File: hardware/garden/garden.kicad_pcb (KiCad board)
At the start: 4 copper layers, 99.7 x 99.7 mm, 111 parts, among them J1 CONN_01X04, J10 CONN_01X09, J2 CONN_01X02, J3 CONN_01X02, J4 CONN_01X02, J5 CONN_01X02, J6 CONN_01X02, J7 CONN_01X04, J8 CONN_01X04, J9 USB_B_Micro, M2 CONN_01X01, M3 CONN_01X01, M4 CONN_01X01, M5 CONN_01X01, Q1 Q_NPN_BEC, Q2 Q_NMOS_GDS, Q3 Q_NMOS_GDS, Q4 Q_NPN_BEC, Q5 Q_NMOS_GDS, SW1 SW_Push, U1 INA226, U10 DHT11, U11 AZ1117-3.3, U12 MCP1416, U13 MCP1416, U14 MCP1416, U2 INA226, U3 CP2102, U4 ESP32-WROOM-32, U5 INA226, U7 MCP1416, U9 MP2451DT

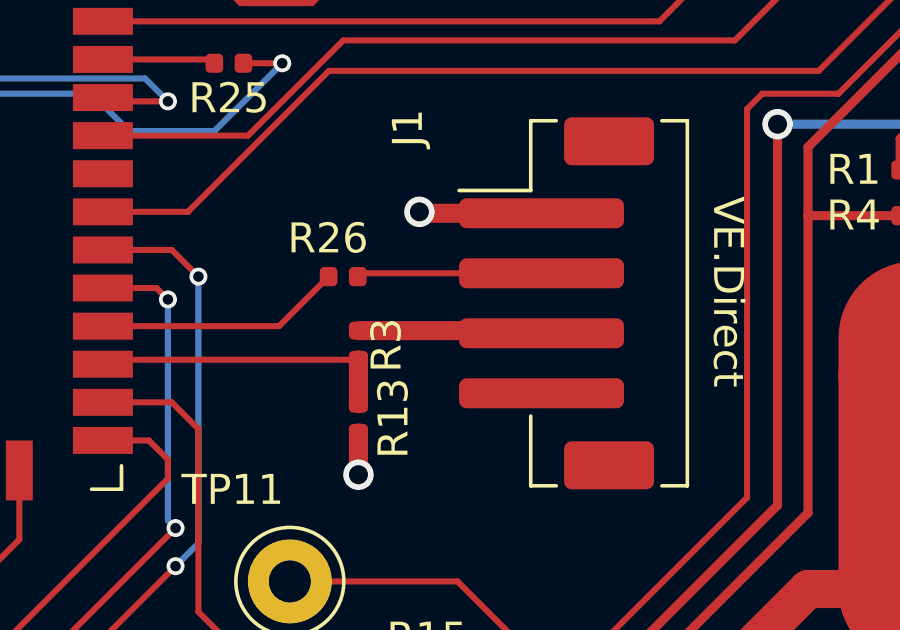
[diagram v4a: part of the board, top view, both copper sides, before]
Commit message: Fixed VE.Direct pinout
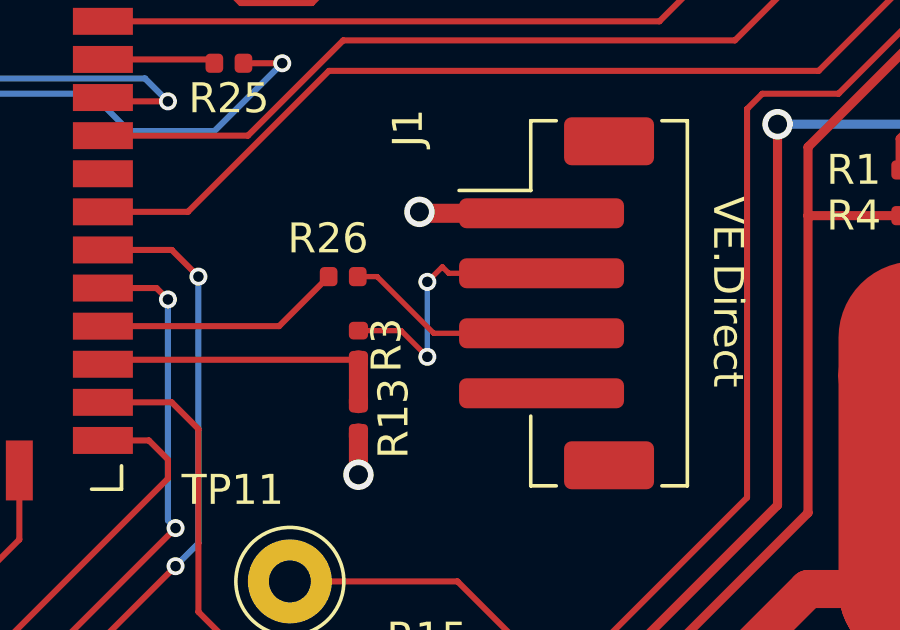
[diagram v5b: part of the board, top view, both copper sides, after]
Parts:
- C6: value 0.1uF -> 4.7uF
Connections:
- J1 pad 2: /VD_RX -> Net-(J1-Pad2)
- J1 pad 3: Net-(J1-Pad3) -> /VD_RX
- J1 pad 4: (no net) -> Net-(J1-Pad4)
- J9 pad 4: (no net) -> Net-(J9-Pad4)
- M2 pad 1: (no net) -> Net-(M2-Pad1)
- M3 pad 1: (no net) -> Net-(M3-Pad1)
- M4 pad 1: (no net) -> Net-(M4-Pad1)
- M5 pad 1: (no net) -> Net-(M5-Pad1)
- R3 pad 1: Net-(J1-Pad3) -> Net-(J1-Pad2)
- U10 pad 3: (no net) -> Net-(U10-Pad3)
- U12 pad 1: (no net) -> Net-(U12-Pad1)
- U13 pad 1: (no net) -> Net-(U13-Pad1)
- U14 pad 1: (no net) -> Net-(U14-Pad1)
- U3 pad 1: (no net) -> Net-(U3-Pad1)
- U3 pad 10: (no net) -> Net-(U3-Pad10)
- U3 pad 11: (no net) -> Net-(U3-Pad11)
- U3 pad 12: (no net) -> Net-(U3-Pad12)
- U3 pad 13: (no net) -> Net-(U3-Pad13)
- U3 pad 14: (no net) -> Net-(U3-Pad14)
- U3 pad 15: (no net) -> Net-(U3-Pad15)
- U3 pad 16: (no net) -> Net-(U3-Pad16)
- U3 pad 17: (no net) -> Net-(U3-Pad17)
- U3 pad 18: (no net) -> Net-(U3-Pad18)
- U3 pad 19: (no net) -> Net-(U3-Pad19)
- U3 pad 2: (no net) -> Net-(U3-Pad2)
- U3 pad 20: (no net) -> Net-(U3-Pad20)
- U3 pad 21: (no net) -> Net-(U3-Pad21)
- U3 pad 22: (no net) -> Net-(U3-Pad22)
- U3 pad 23: (no net) -> Net-(U3-Pad23)
- U3 pad 27: (no net) -> Net-(U3-Pad27)
- U4 pad 13: (no net) -> Net-(U4-Pad13)
- U4 pad 17: (no net) -> Net-(U4-Pad17)
- U4 pad 18: (no net) -> Net-(U4-Pad18)
- U4 pad 19: (no net) -> Net-(U4-Pad19)
- U4 pad 20: (no net) -> Net-(U4-Pad20)
- U4 pad 21: (no net) -> Net-(U4-Pad21)
- U4 pad 22: (no net) -> Net-(U4-Pad22)
- U4 pad 23: (no net) -> Net-(U4-Pad23)
- U4 pad 32: (no net) -> Net-(U4-Pad32)
- U7 pad 1: (no net) -> Net-(U7-Pad1)
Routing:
- net Net-(J1-Pad2): track 0.00 -> 9.26 mm, vias 0 -> 2
- net Net-(J1-Pad3): track 6.14 -> 0.00 mm
- net /VD_RX: track 6.17 -> 6.91 mm

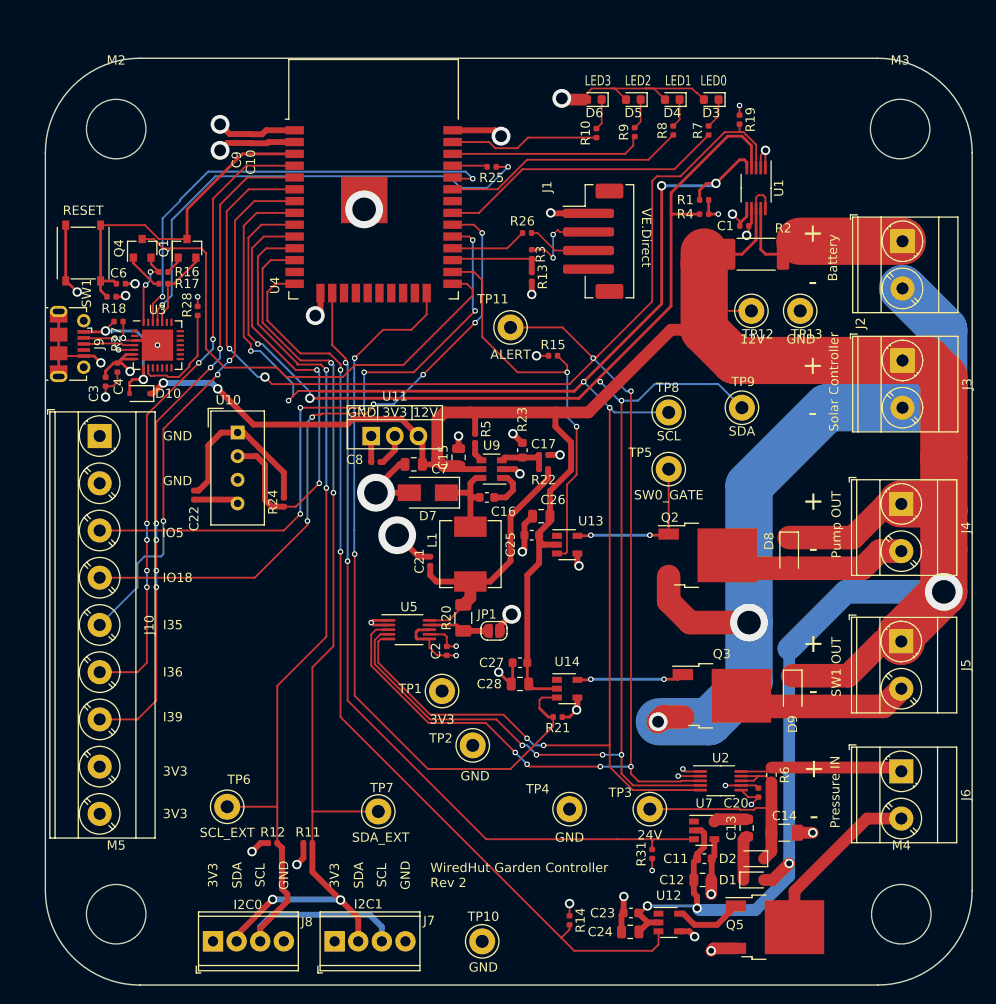
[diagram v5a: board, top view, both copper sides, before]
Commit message: Added v3 garden controller hardware
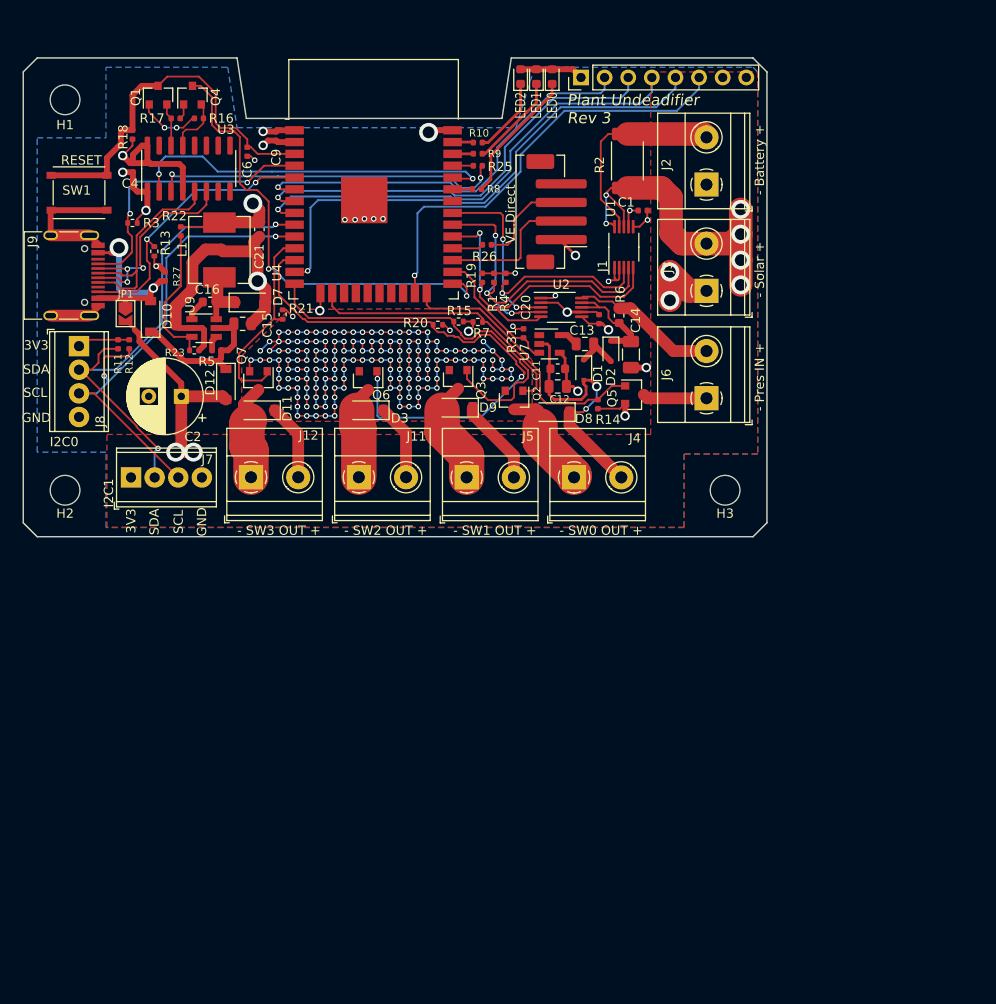
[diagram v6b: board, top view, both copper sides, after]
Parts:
- removed C10, C22: 0.1uF, Capacitor_SMD:C_0402_1005Metric
- removed C17: 33pF, Capacitor_SMD:C_0402_1005Metric
- removed C23, C25, C27: 0.1uF/50V, Capacitor_SMD:C_0603_1608Metric
- removed C24, C26, C28: 1uF/50V, Capacitor_SMD:C_0805_2012Metric
- removed C3: 1uF, Capacitor_SMD:C_0402_1005Metric
- removed C7: 22uF, Capacitor_SMD:C_0805_2012Metric
- removed C8: 10uF, Capacitor_SMD:C_0402_1005Metric
- removed M2, M3, M4, M5: CONN_01X01, MountingHole:MountingHole_6.4mm_M6
- removed R24, R28: 10kR, Resistor_SMD:R_0402_1005Metric
- removed TP1, TP10, TP11, TP12, TP13, TP2, TP3, TP4, TP5, TP6, TP7, TP8, TP9: TestPoint, TestPoint:TestPoint_Loop_D3.50mm_Drill1.4mm_Beaded
- removed U10: DHT11, Sensor:Aosong_DHT11_5.5x12.0_P2.54mm
- removed U11: AZ1117-3.3, Package_TO_SOT_THT:TO-220-3_Vertical
- removed U12, U13, U14: MCP1416, Package_TO_SOT_SMD:SOT-23-5
- removed U5: INA226, Package_SO:VSSOP-10_3x3mm_P0.5mm
- added D11: D_Schottky, Diode_SMD:D_SOD-123, F.Cu at (78.9, 87.4)
- added D12: D_Schottky, Diode_SMD:D_SOD-123, F.Cu at (75.3, 84.6)
- added H1: MountingHole, MountingHole:MountingHole_3.2mm_M3, F.Cu at (58.0, 54.0)
- added H2: MountingHole, MountingHole:MountingHole_3.2mm_M3, F.Cu at (58.0, 96.0)
- added H3: MountingHole, MountingHole:MountingHole_3.2mm_M3, F.Cu at (129.0, 96.0)
- added J11: CONN_01X02, TerminalBlock_Phoenix:TerminalBlock_Phoenix_MKDS-1,5-2-5.08_1x02_P5.08mm_Horizontal, F.Cu at (89.6, 94.6)
- added J12: CONN_01X02, TerminalBlock_Phoenix:TerminalBlock_Phoenix_MKDS-1,5-2-5.08_1x02_P5.08mm_Horizontal, F.Cu at (78.0, 94.6)
- added Q6: AO3416, Package_TO_SOT_SMD:SOT-23, F.Cu at (90.6, 84.2)
- added Q7: AO3416, Package_TO_SOT_SMD:SOT-23, F.Cu at (78.8, 84.2)
- C15: value 22uF -> 10uF
- C2: value 0.1uF -> 220uF/25V; footprint Capacitor_SMD:C_0402_1005Metric -> Capacitor_THT:CP_Radial_D8.0mm_P3.50mm
- C21: value 10uF -> 22uF; footprint Capacitor_SMD:C_0402_1005Metric -> Capacitor_SMD:C_0603_1608Metric
- D1, D2: value D -> 1N4148
- D10: value D -> D_Schottky; footprint Diode_SMD:D_SOD-323F -> Diode_SMD:D_SOD-123
- D3: value GREEN -> D_Schottky; footprint LED_SMD:LED_0603_1608Metric -> Diode_SMD:D_SOD-123
- D7: footprint Diode_SMD:D_SMA -> Diode_SMD:D_SOD-123
- J10: value CONN_01X09 -> CONN_01X08; footprint TerminalBlock_Phoenix:TerminalBlock_Phoenix_MKDS-3-9-5.08_1x09_P5.08mm_Horizontal -> Connector_PinHeader_2.54mm:PinHeader_1x08_P2.54mm_Vertical
- J2, J3, J4, J5, J6: footprint TerminalBlock_Phoenix:TerminalBlock_Phoenix_MKDS-3-2-5.08_1x02_P5.08mm_Horizontal -> TerminalBlock_Phoenix:TerminalBlock_Phoenix_MKDS-1,5-2-5.08_1x02_P5.08mm_Horizontal
- J9: value USB_B_Micro -> USB_C_Receptacle_USB2.0; footprint Connector_USB:USB_Micro-B_Molex-105017-0001 -> Connector_USB:USB_C_Receptacle_HRO_TYPE-C-31-M-12
- JP1: value Jumper -> SolderJumper_2_Open; footprint Jumper:SolderJumper-2_P1.3mm_Open_RoundedPad1.0x1.5mm -> Jumper:SolderJumper-2_P1.3mm_Open_TrianglePad1.0x1.5mm
- Q2, Q3: value Q_NMOS_GDS -> AO3416; footprint Package_TO_SOT_SMD:TO-252-2 -> Package_TO_SOT_SMD:SOT-23
- Q5: value Q_NMOS_GDS -> Q_NMOS_GSD/30V; footprint Package_TO_SOT_SMD:TO-252-2 -> Package_TO_SOT_SMD:SOT-23
- R13: value 2kR -> 5.1k
- R20: value 0.1R -> 10kR; footprint Resistor_SMD:R_1206_3216Metric -> Resistor_SMD:R_0402_1005Metric
- R22: value 124kR -> 49.9k
- R23: value 40.2kR -> 16.2k; footprint Resistor_SMD:R_0603_1608Metric -> Resistor_SMD:R_0402_1005Metric
- R3: value 1kR -> 5.1k
- R7: value 100R -> 10kR
- U3: value CP2102 -> CH340C; footprint Package_DFN_QFN:QFN-28-1EP_5x5mm_P0.5mm_EP3.35x3.35mm -> Package_SO:SOIC-16_3.9x9.9mm_P1.27mm
- U9: value MP2451DT -> MP2359; footprint Package_TO_SOT_SMD:SOT-23-6 -> Package_TO_SOT_SMD:TSOT-23-6
- moved J8 65.6 mm to (59.5, 80.5), turned to 270 degrees
- moved J10 64.6 mm to (113.5, 51.6), turned to 90 degrees
- moved Q5 59.2 mm to (119.3, 85.7)
- moved D1 57.8 mm to (113.8, 83.1), turned to 270 degrees
- moved R31 57.7 mm to (107.3, 79.1), turned to 270 degrees
- moved R11 57.4 mm to (63.7, 80.3), turned to 270 degrees
- moved D2 56.7 mm to (116.7, 81.0), turned to 270 degrees
- moved R12 55.8 mm to (64.9, 80.3), turned to 270 degrees
- moved R14 55.6 mm to (115.3, 86.7), turned to 90 degrees
- moved C12 55.3 mm to (111.0, 84.8)
- moved C11 55.0 mm to (111.0, 82.9)
- moved U7 54.9 mm to (110.1, 80.3)
- moved C13 54.9 mm to (113.9, 80.3), turned to 180 degrees
- moved J7 54.5 mm to (65.1, 94.6)
- moved C14 54.0 mm to (118.9, 81.4), turned to 270 degrees
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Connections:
- net /PRES_SHUNT_P renamed Net-(C14-Pad1)
- C15 pad 1: +12V -> Net-(C15-Pad1)
- C2 pad 1: +3V3 -> +12V
- C21 pad 1: /3V3_SHUNT_P -> +3V3
- D10 pad 1: +12V -> Net-(C15-Pad1)
- D10 pad 2: Net-(D10-Pad2) -> /Vbus
- D3 pad 1: Net-(D3-Pad1) -> +12V
- D3 pad 2: +3V3 -> Net-(D3-Pad2)
- J1 pad 2: Net-(J1-Pad2) -> /VD_TX
- J1 pad 4: Net-(J1-Pad4) -> (no net)
- J10 pad 1: GND -> +3V3
- J10 pad 2: GND -> /IO34
- J10 pad 3: /IO5 -> /IO35
- J10 pad 4: /IO18 -> /IO32
- J10 pad 5: /I35 -> /IO14
- J10 pad 6: /I36 -> /IO15
- J10 pad 7: /I39 -> +12V
- J10 pad 8: +3V3 -> GND
- J2 pad 1: /BATT_SHUNT_N -> GND
- J2 pad 2: GND -> /BATT_SHUNT_N
- J3 pad 1: +12V -> GND
- J3 pad 2: GND -> +12V
- J4 pad 1: +12V -> Net-(D8-Pad2)
- J4 pad 2: Net-(D8-Pad2) -> +12V
- J5 pad 1: +12V -> Net-(D9-Pad2)
- J5 pad 2: Net-(D9-Pad2) -> +12V
- J6 pad 1: /PRES_SHUNT_N -> Net-(J6-Pad1)
- JP1 pad 1: /3V3_SHUNT_N -> /Vbus
- JP1 pad 2: +3V3 -> +12V
- L1 pad 2: /3V3_SHUNT_P -> +3V3
- Q2 pad 1: /SW0_GATE -> /SW0
- Q2 pad 2: Net-(D8-Pad2) -> GND
- Q2 pad 3: GND -> Net-(D8-Pad2)
- Q3 pad 1: /SW1_GATE -> /SW1
- Q3 pad 2: Net-(D9-Pad2) -> GND
- Q3 pad 3: GND -> Net-(D9-Pad2)
- Q5 pad 1: /PRESSURE_SW_GATE -> /PRESSURE_SW
- Q5 pad 2: Net-(J6-Pad2) -> GND
- Q5 pad 3: GND -> Net-(J6-Pad1)
- R1 pad 2: /SCL -> /SDA
- R10 pad 1: /LED3 -> /LED2
- R13 pad 1: /VD_TX -> /CC2
- R15 pad 2: /SW0 -> /SW1
- R19 pad 2: /ALERT -> /SCL
- R20 pad 1: /3V3_SHUNT_N -> GND
- R20 pad 2: /3V3_SHUNT_P -> /SW2
- R21 pad 2: /SW1 -> /SW3
- R22 pad 1: /3V3_SHUNT_P -> +3V3
- R27 pad 2: Net-(D10-Pad2) -> /Vbus
- R3 pad 1: Net-(J1-Pad2) -> /CC1
- R3 pad 2: /VD_TX -> GND
- R4 pad 2: /SDA -> /ALERT
- R5 pad 1: +12V -> Net-(C15-Pad1)
- R6 pad 1: /PRES_SHUNT_N -> Net-(J6-Pad2)
- R7 pad 1: /LED0 -> GND
- R7 pad 2: Net-(D3-Pad1) -> /SW0
- R8 pad 1: /LED1 -> /LED0
- R9 pad 1: /LED2 -> /LED1
- U2 pad 10: /PRES_SHUNT_N -> Net-(J6-Pad2)
- U3 pad 1: Net-(U3-Pad1) -> GND
- U3 pad 10: Net-(U3-Pad10) -> (no net)
- U3 pad 11: Net-(U3-Pad11) -> (no net)
- U3 pad 12: Net-(U3-Pad12) -> (no net)
- U3 pad 13: Net-(U3-Pad13) -> /USB_DTR
- U3 pad 14: Net-(U3-Pad14) -> /USB_RTS
- U3 pad 15: Net-(U3-Pad15) -> (no net)
- U3 pad 16: Net-(U3-Pad16) -> +3V3
- U3 pad 2: Net-(U3-Pad2) -> /USB_TX
- U3 pad 3: GND -> /USB_RX
- U3 pad 4: Net-(J9-Pad3) -> +3V3
- U3 pad 5: Net-(J9-Pad2) -> /Dp
- U3 pad 6: +3V3 -> /Dm
- U3 pad 7: +3V3 -> (no net)
- U3 pad 8: Net-(D10-Pad2) -> (no net)
- U3 pad 9: Net-(R28-Pad1) -> (no net)
- U4 pad 10: /DHT22 -> /SCL_EXT
- U4 pad 11: /SCL_EXT -> /SW3
- U4 pad 12: /SDA_EXT -> /SW2
- U4 pad 13: Net-(U4-Pad13) -> /IO14
- U4 pad 14: /PRESSURE_SW -> /SW1
- U4 pad 16: /PRESSURE_PWR -> /SW0
- U4 pad 17: Net-(U4-Pad17) -> (no net)
- U4 pad 18: Net-(U4-Pad18) -> (no net)
- U4 pad 19: Net-(U4-Pad19) -> (no net)
- U4 pad 20: Net-(U4-Pad20) -> (no net)
- U4 pad 21: Net-(U4-Pad21) -> (no net)
- U4 pad 22: Net-(U4-Pad22) -> (no net)
- U4 pad 23: Net-(U4-Pad23) -> /IO15
- U4 pad 24: /SW1 -> /PRESSURE_SW
- U4 pad 26: /SW0 -> /PRESSURE_PWR
- U4 pad 29: /IO5 -> /SCL
- U4 pad 30: /IO18 -> /SDA
- U4 pad 31: /LED0 -> /ALERT
- U4 pad 32: Net-(U4-Pad32) -> (no net)
- U4 pad 33: /LED1 -> /LED0
- U4 pad 36: /LED2 -> /LED1
- U4 pad 37: /LED3 -> /LED2
- U4 pad 4: /I36 -> /CC1
- U4 pad 5: /I39 -> /CC2
- U4 pad 6: /ALERT -> /IO34
- U4 pad 7: /I35 -> /IO35
- U4 pad 8: /SCL -> /IO32
- U4 pad 9: /SDA -> /SDA_EXT
- U7 pad 1: Net-(U7-Pad1) -> (no net)
- U9 pad 5: +12V -> Net-(C15-Pad1)
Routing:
- net +12V: track 319.0 -> 114.5 mm, vias 6 -> 10
- net /ALERT: track 207.4 -> 36.1 mm, vias 8 -> 3
- net /SDA: track 200.3 -> 40.1 mm, vias 8 -> 3
- net /SCL: track 191.1 -> 37.5 mm, vias 8 -> 2
- net /PRESSURE_PWR: track 89.1 -> 14.2 mm, vias 2 -> 0
- net GND: track 215.6 -> 289.7 mm, vias 38 -> 188
- net /PRESSURE_SW: track 102.2 -> 29.6 mm, vias 2 -> 0
- net /I39: track 72.3 -> 0.00 mm, vias 6 -> 0
- net /IO18: track 71.9 -> 0.00 mm, vias 6 -> 0
- net /IO5: track 69.0 -> 0.00 mm, vias 6 -> 0
- net /I36: track 68.6 -> 0.00 mm, vias 6 -> 0
- net /SW2: track 0.00 -> 58.9 mm, vias 0 -> 2
- net /I35: track 57.9 -> 0.00 mm, vias 3 -> 0
- net /IO14: track 0.00 -> 55.6 mm, vias 0 -> 1
- net /SCL_EXT: track 109.1 -> 55.0 mm
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- added copper zone on F.Cu, net +12V
- added copper zone on Vcc.Cu, net +12V
- added copper zone on B.Cu, net GND
- added copper zone on F.Cu, net GND
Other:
- board size 99.7 x 99.7 mm -> 80 x 51.5 mm
- net class Default: trace_width 0.1778 -> 0.2032
- board text added: "- Battery +"
- board text added: "- Pres IN +"
- board text added: "- SW0 OUT +"
- board text added: "- SW1 OUT +"
- board text added: "- SW2 OUT +"
- board text added: "- SW3 OUT +"
- board text added: "- Solar +"
- board text added: "Dubious Creations https://dubiouscreations.com"
- board text added: "Plant Undeadifier Rev 3"
- board text removed: "+"
- board text removed: "-"
- board text removed: "12V"
- board text removed: "24V"
- board text removed: "ALERT"
- board text removed: "Battery"
- board text removed: "I35"
- board text removed: "I36"
- board text removed: "I39"
- board text removed: "IO18"
- board text removed: "IO5"
- board text removed: "LED3"
- board text removed: "Pressure IN"
- board text removed: "Pump OUT"
- board text removed: "SCL_EXT"
- board text removed: "SDA_EXT"
- board text removed: "SW0_GATE"
- board text removed: "SW1 OUT"
- board text removed: "Solar Controller"
- board text removed: "WiredHut Garden Controller Rev 2"

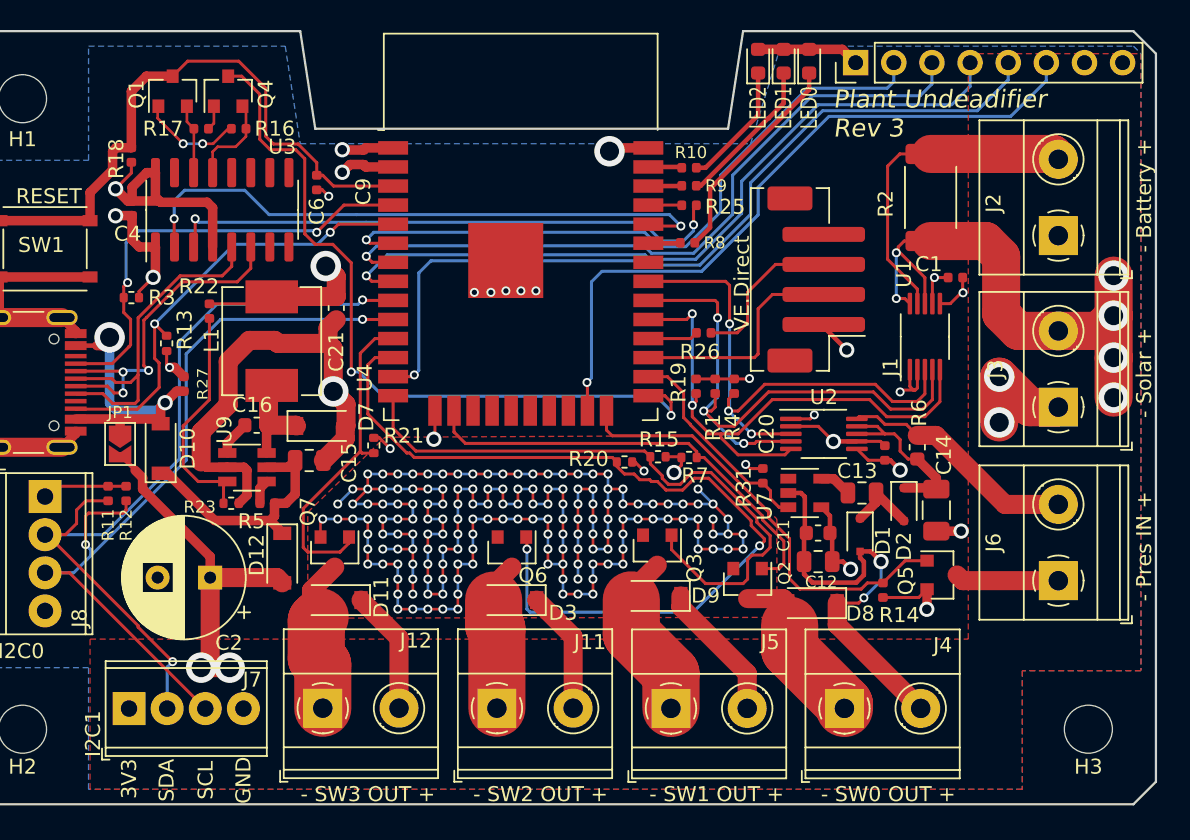
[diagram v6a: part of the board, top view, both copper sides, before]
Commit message: Updated garden and temp sensor hw
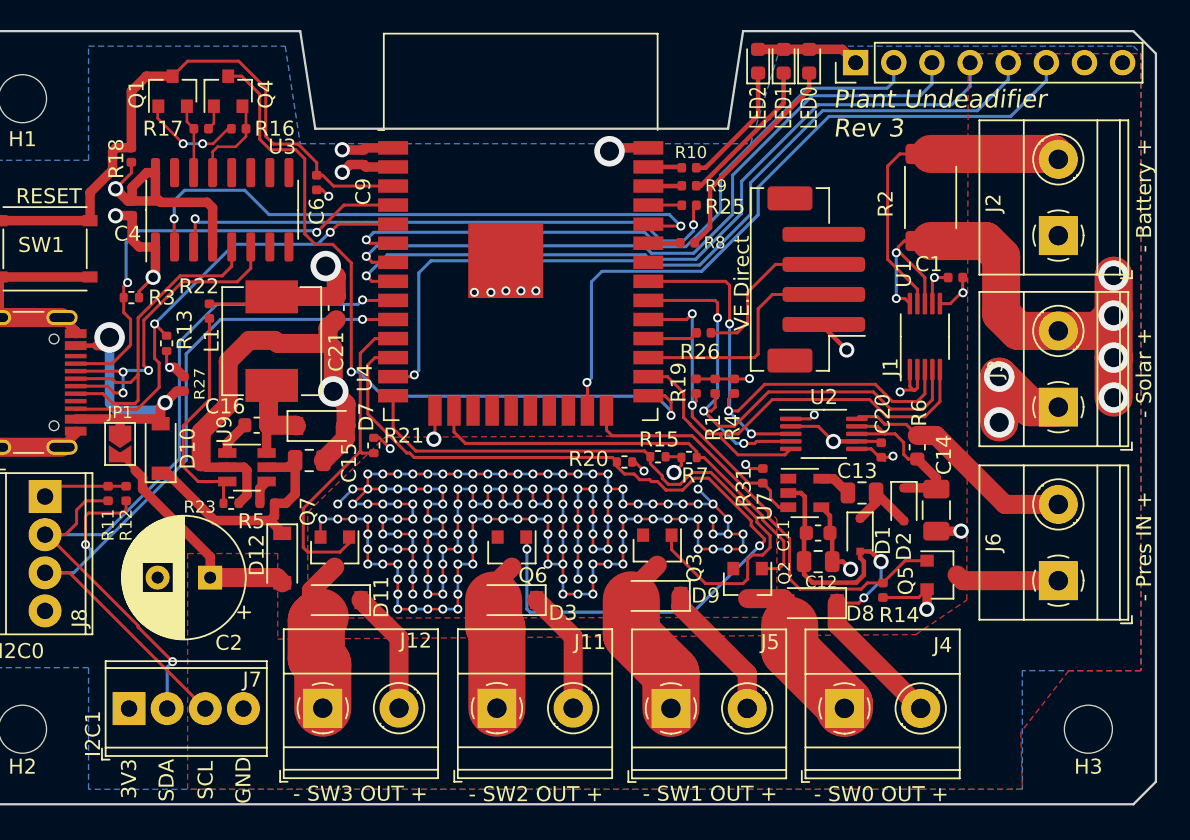
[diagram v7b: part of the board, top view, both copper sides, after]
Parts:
- moved C20 0.31 mm to (115.2, 77.4)
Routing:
- net +12V: track 114.5 -> 106.3 mm, vias 10 -> 8
- net +3V3: track 55.6 -> 54.8 mm
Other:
- rule pad_to_mask_clearance: 0.2 -> 0
